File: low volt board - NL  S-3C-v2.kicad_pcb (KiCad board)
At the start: 2 copper layers, 124.5 x 73.7 mm, 44 parts, among them J1 ESP32-S3-ETH-WAVETREE-Footpri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, J2 ILI9341 TFT 2.8" Display with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, J3 4 Channel 5v Relay Connector, J4 SPDT (on)-off-(on), J5 ADC Inputs - 24v side, J6 Dry Contact OptoCoupler, J8 5vIn, Q1-Buzzer1 S8050, SW1 SW_SPDT, U1 ADS1115IDGS - low volt, U2 ADS1115IDGS - 24v, U3-Opto1 PC817

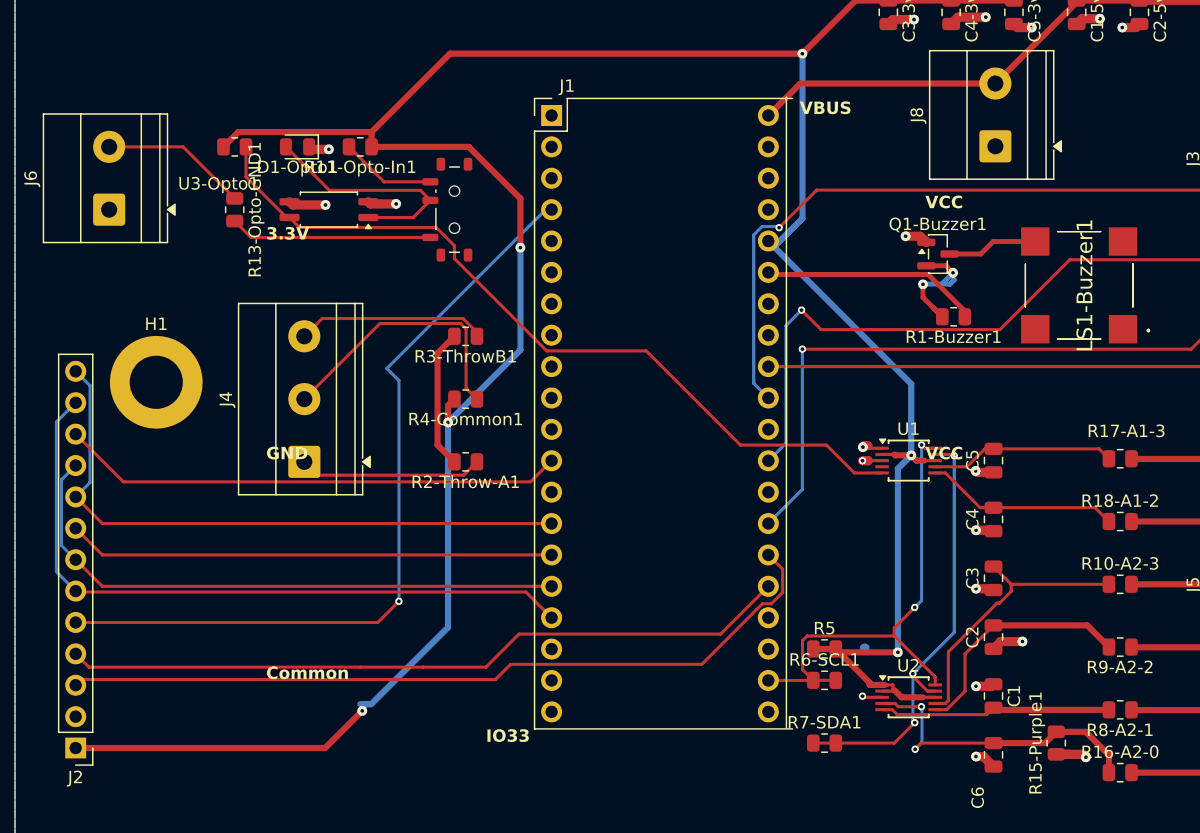
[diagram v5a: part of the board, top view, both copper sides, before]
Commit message: Minor fixes including missing nets
Co-Authored-By: Claude Opus 4.6 <noreply@anthropic.com>
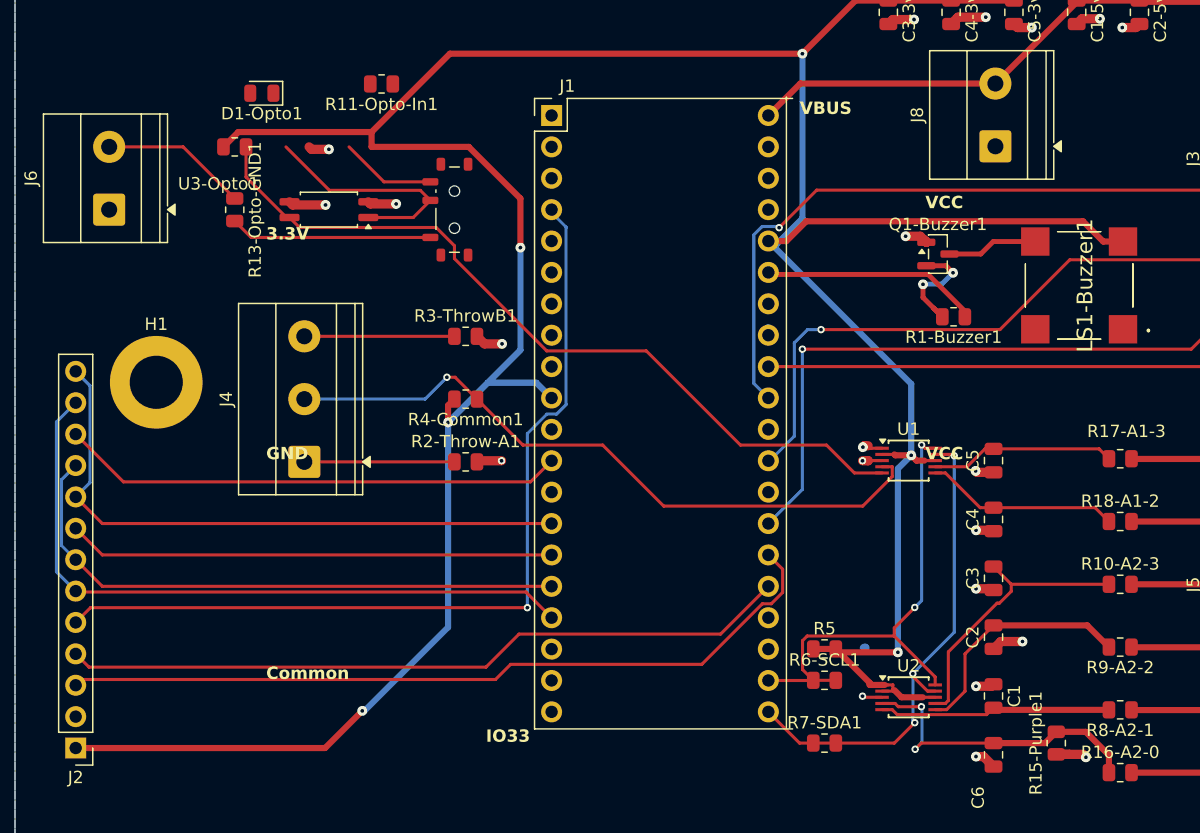
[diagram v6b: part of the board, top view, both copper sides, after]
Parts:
- moved R11-Opto-In1 5.37 mm to (83.0, 48.2)
- moved D1-Opto1 5.21 mm to (73.3, 49.0)
- turned R2-Throw-A1 to 0 degrees
- turned R3-ThrowB1 to 0 degrees
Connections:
- J1 pad 10: unconnected-(J1-GPIO41-Pad10) -> +3.3V
- J1 pad 13: unconnected-(J1-GND-Pad13) -> GND
- J1 pad 21: /SCD -> /SDA
- J1 pad 30: unconnected-(J1-CHIP_UP-Pad30) -> GND
- J1 pad 33: unconnected-(J1-GND-Pad33) -> GND
- J1 pad 8: unconnected-(J1-GND-Pad8) -> GND
- J4 pad 2: /IO17 -> /A1-0
- LS1-Buzzer1 pad 2: /3v Clean -> +3.3V
- R2-Throw-A1 pad 2: /GND - 3v Clean -> GND
- R3-ThrowB1 pad 2: /GND - 3v Clean -> GND
- R4-Common1 pad 1: /IO17 -> /A1-0
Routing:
- net /A1-0: track 0.00 -> 55.2 mm, vias 0 -> 1
- net +3.3V: track 235.3 -> 270.5 mm
- net /IO17: track 21.8 -> 0.00 mm
- net /GND - 3v Clean: track 11.3 -> 0.00 mm
- net /IO48: track 64.8 -> 72.1 mm
- net GND: track 38.3 -> 43.7 mm, vias 19 -> 21
- net /SDA: track 36.0 -> 40.7 mm
- net /Rnet2: track 15.4 -> 12.2 mm
- net /IO15: track 54.5 -> 52.3 mm
- net /Buzzer-2: track 10.7 -> 9.48 mm
- net /Rnet1: track 14.9 -> 13.7 mm
- net /A2-0: track 26.6 -> 25.4 mm

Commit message: Ready for fabrication review
Co-Authored-By: Claude Opus 4.6 <noreply@anthropic.com>
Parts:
- moved R1-Buzzer1 6.60 mm to (123.8, 63.5)
- turned R7-SDA1 to 180 degrees
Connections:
- net /Buzzer-3 renamed Net-(LS1-Buzzer1--LEAD)
- J1 pad 10: +3.3V -> /IO41
- J1 pad 28: unconnected-(J1-GND-Pad28) -> GND
- J1 pad 35: /Buzer-IO21 -> /IO21
- Q1-Buzzer1 pad 1: GND -> Net-(Q1-Buzzer1-E)
- Q1-Buzzer1 pad 2: /Buzzer-2 -> GND
- R1-Buzzer1 pad 1: /Buzer-IO21 -> Net-(Q1-Buzzer1-E)
- R1-Buzzer1 pad 2: /Buzzer-2 -> /IO21
- R5 pad 1: +3.3V -> /IO41
- R6-SCL1 pad 1: /SCL -> /SCL-In
- R7-SDA1 pad 1: /SDA -> /SDA-In
- U1 pad 10: /SCL -> /SCL-In
- U1 pad 2: +3.3V -> /IO41
- U1 pad 9: /SDA -> /SDA-In
- U2 pad 10: /SCL -> /SCL-In
- U2 pad 2: +3.3V -> /IO41
- U2 pad 9: /SDA -> /SDA-In
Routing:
- net /IO41: track 0.00 -> 81.2 mm, vias 0 -> 2
- net /SDA: track 40.7 -> 4.68 mm, vias 3 -> 0
- net /SDA-In: track 0.00 -> 34.2 mm, vias 0 -> 3
- net /SCL-In: track 0.00 -> 34.1 mm, vias 0 -> 2
- net /SCL: track 39.5 -> 7.26 mm, vias 2 -> 0
- net /Buzer-IO21: track 17.8 -> 0.00 mm
- net +3.3V: track 270.5 -> 257.4 mm
- net Net-(D1-Opto1-A): track 19.1 -> 30.7 mm, vias 0 -> 2
- net Net-(SW1-C): track 7.75 -> 17.3 mm, vias 0 -> 2
- net /Buzzer-2: track 9.48 -> 0.00 mm, vias 2 -> 0
- net /IO21: track 0.00 -> 8.77 mm
- net Net-(Q1-Buzzer1-E): track 0.00 -> 3.44 mm
- net GND: track 43.7 -> 40.3 mm
- net /A2-0: track 25.4 -> 26.6 mm
- net /A1-3: track 15.0 -> 14.3 mm
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
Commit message: v2 ready for production
Co-Authored-By: Claude Opus 4.6 <noreply@anthropic.com>
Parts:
- moved R7-SDA1 2.34 mm to (118.8, 99.2)
- turned R6-SCL1 to 180 degrees
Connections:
- R6-SCL1 pad 1: /SCL-In -> +3.3V
- R7-SDA1 pad 1: /SDA-In -> +3.3V
- U1 pad 10: /SCL-In -> /SCL
- U1 pad 9: /SDA-In -> /SDA
- U2 pad 10: /SCL-In -> /SCL
- U2 pad 9: /SDA-In -> /SDA
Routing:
- net /SDA: track 4.68 -> 44.6 mm, vias 0 -> 3
- net /SDA-In: track 34.2 -> 0.00 mm, vias 3 -> 0
- net /SCL-In: track 34.1 -> 0.00 mm, vias 2 -> 0
- net /SCL: track 7.26 -> 37.7 mm, vias 0 -> 2
- net +3.3V: track 257.4 -> 262.7 mm
- net /IO41: track 81.2 -> 81.1 mm, vias 2 -> 3
